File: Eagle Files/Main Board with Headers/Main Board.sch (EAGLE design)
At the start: 34 parts, among them Y1 16MHz

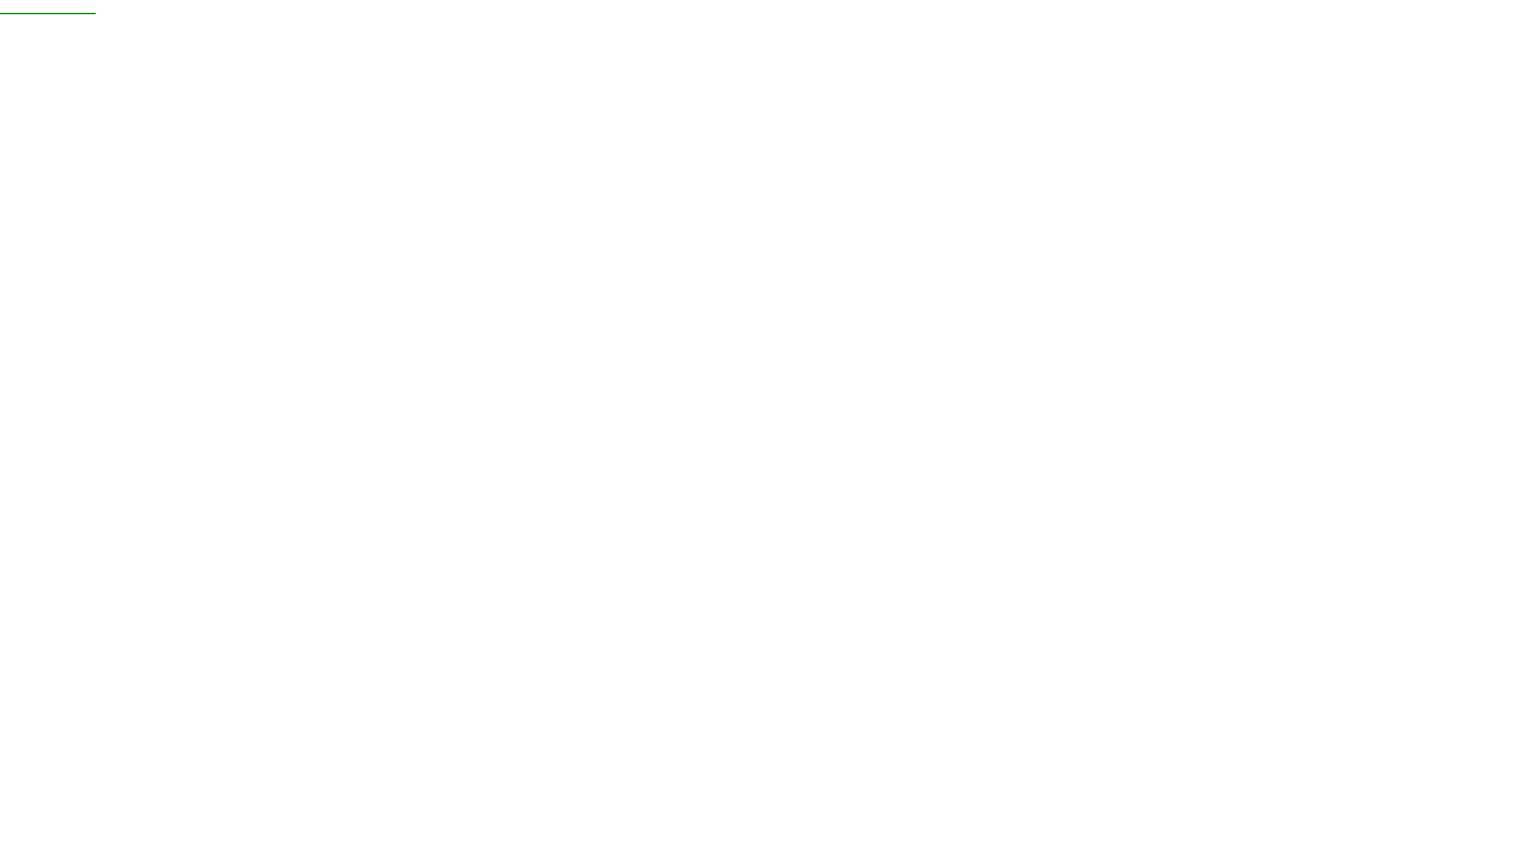
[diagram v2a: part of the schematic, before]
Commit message: Panelized the Radio board and Main Board.
Basically main Board with Headers is being turned into the new Main Board.
I've already attached the SD Card holder.
Next step is to integrate these two boards, instead of just panelizing them.

--Arthur

git-svn-id: http://cd-net.net/CPE496/trunk@116 05b6d0e0-c345-4a8e-a5b7-579c8bd0b646
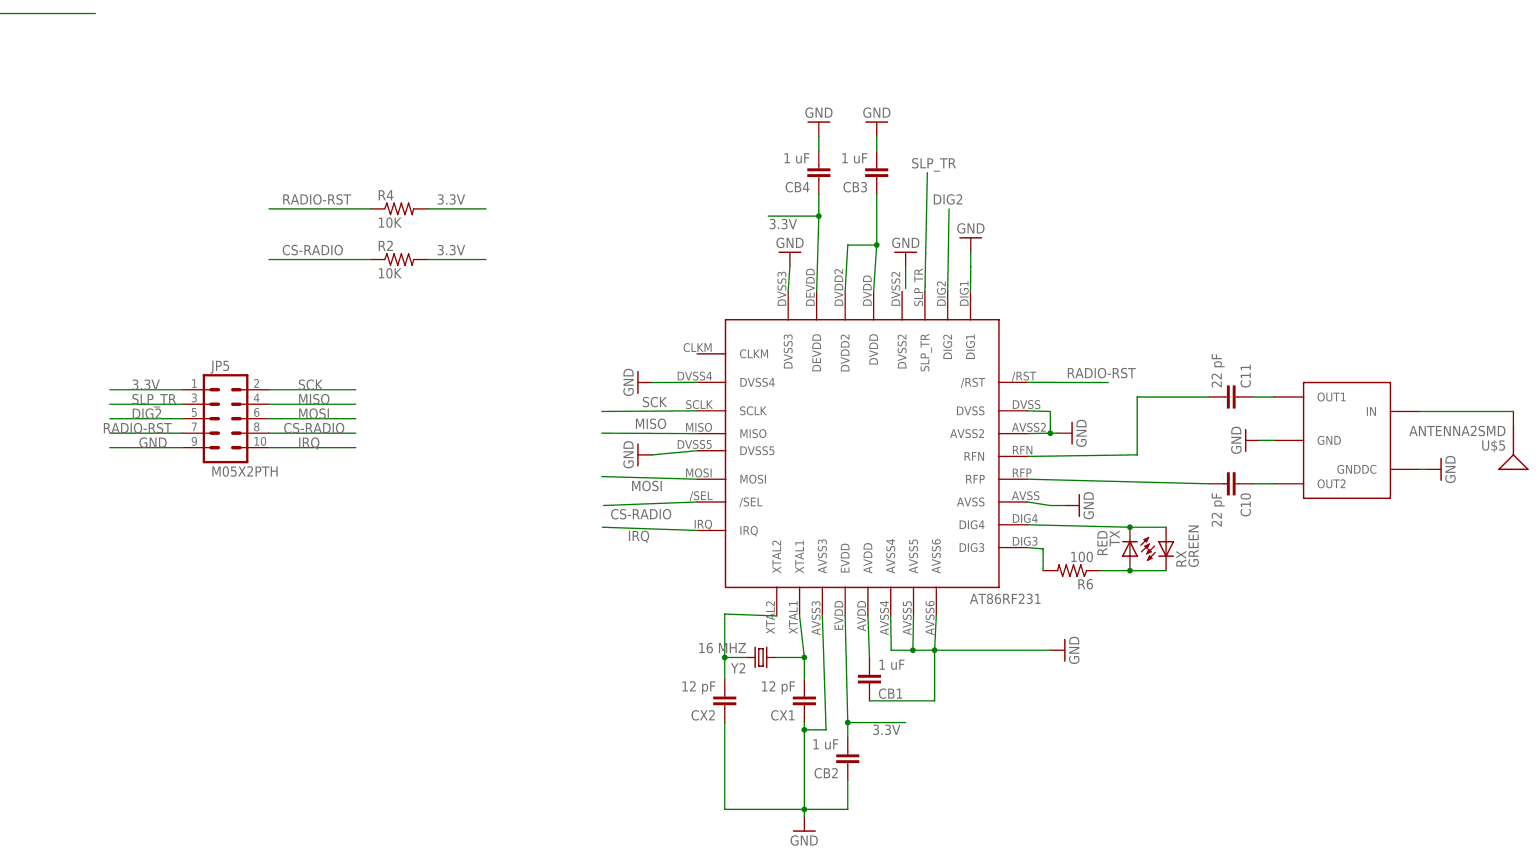
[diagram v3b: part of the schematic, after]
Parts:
- added C10, C11: 22 pF, SparkFun:CAP0603-CAP
- added CB1, CB2, CB3, CB4: 1 uF, SparkFun:CAP0603-CAP
- added CX1, CX2: 12 pF, SparkFun:CAP0603-CAP
- added JP5: M05X2PTH, SparkFun:M05X2PTH
- added R2, R4: 10K, SparkFun:RESISTOR0603-RES
- added R6: 100, SparkFun:RESISTOR0603-RES
- added RX: GREEN, SparkFun:LED0603
- added TX: RED, SparkFun:LED0603
- added U$3: AT86RF231(RADIO)AT86RF231, group10:AT86RF231(RADIO)AT86RF231
- added U$4: WE-BAL, group10:WE-BAL
- added U$5: ANTENNA2SMD, SparkFun:ANTENNA2SMD
- added Y2: 16 MHZ, group10:CRYSTALSMD
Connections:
- new net N$10: CB1.2, U$3.AVDD
- new net N$11: CX1.2, U$3.XTAL1, Y2.1
- new net N$12: CX2.2, U$3.XTAL2, Y2.2
- new net N$13: RX.A, TX.C, U$3.DIG4
- new net N$14: R6.1, RX.C, TX.A
- new net N$15: R6.2, U$3.DIG3
- new net N$16: C10.1, U$4.OUT2
- new net N$17: C11.1, U$4.OUT1
- new net N$18: C11.2, U$3.RFN
- new net N$19: C10.2, U$3.RFP
- new net N$20: U$4.IN, U$5.SIGNAL
- new net N$8: CB3.1, U$3.DVDD, U$3.DVDD2
- net 3.3V: now also CB2.2, CB4.1, JP5.1, R2.2, R4.2, U$3.DEVDD, U$3.EVDD
- net CS-RADIO: now also JP5.8, R2.1, U$3./SEL
- net DIG2: now also JP5.5, U$3.DIG2
- net GND: now also CB1.1, CB2.1, CB3.2, CB4.2, CX1.1, CX2.1, JP5.9, U$3.AVSS, U$3.AVSS2, U$3.AVSS3, U$3.AVSS4, U$3.AVSS5, U$3.AVSS6, U$3.DIG1, U$3.DVSS, U$3.DVSS3, U$3.DVSS4, U$3.DVSS5, U$4.GND, U$4.GNDDC
- net IRQ: now also JP5.10, U$3.IRQ
- net MISO: now also JP5.4, U$3.MISO
- net MOSI: now also JP5.6, U$3.MOSI
- net RADIO-RST: now also JP5.7, R4.1, U$3./RST
- net SCK: now also JP5.2, U$3.SCLK
- net SLP_TR: now also JP5.3, U$3.SLP_TR

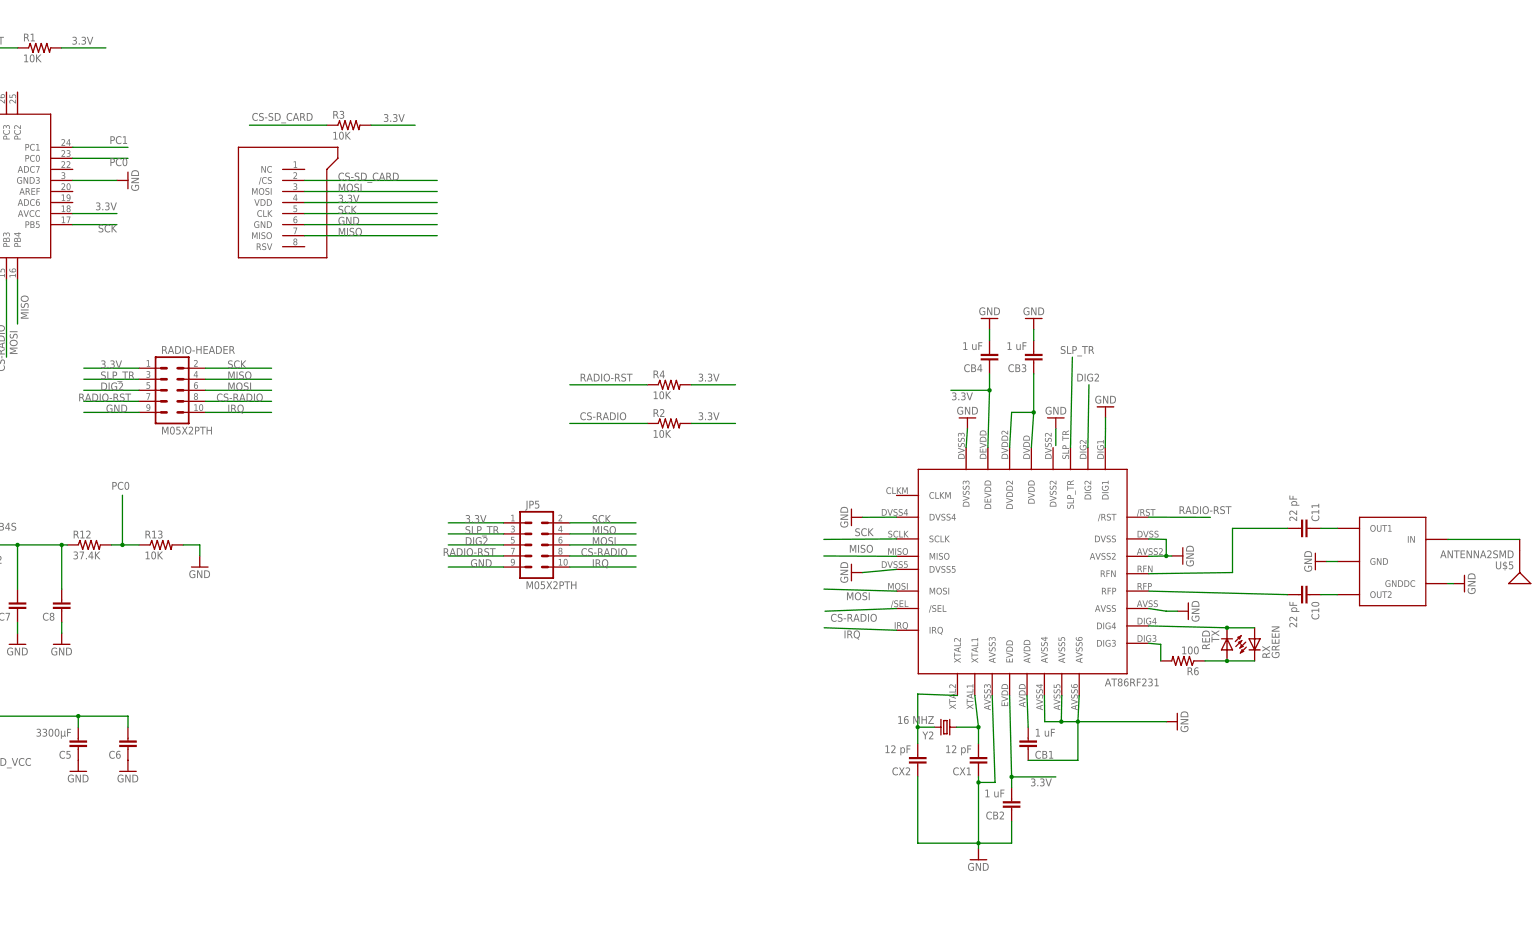
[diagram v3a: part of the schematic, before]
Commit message: Main Board with Headers is now almost ready.
I'm adding the FTDI Module right now.

TODO:
1.  Double check regulator Datasheet.  I think we're missing a capacitor.
2.  Update Radio Module Schematics to incorporate ground plane.
3.  Check if the hall effect sensor can work linearly at 3.3V
4.  Finish Adding FTDI chip and USB connector.

--Arthur

git-svn-id: http://cd-net.net/CPE496/trunk@119 05b6d0e0-c345-4a8e-a5b7-579c8bd0b646
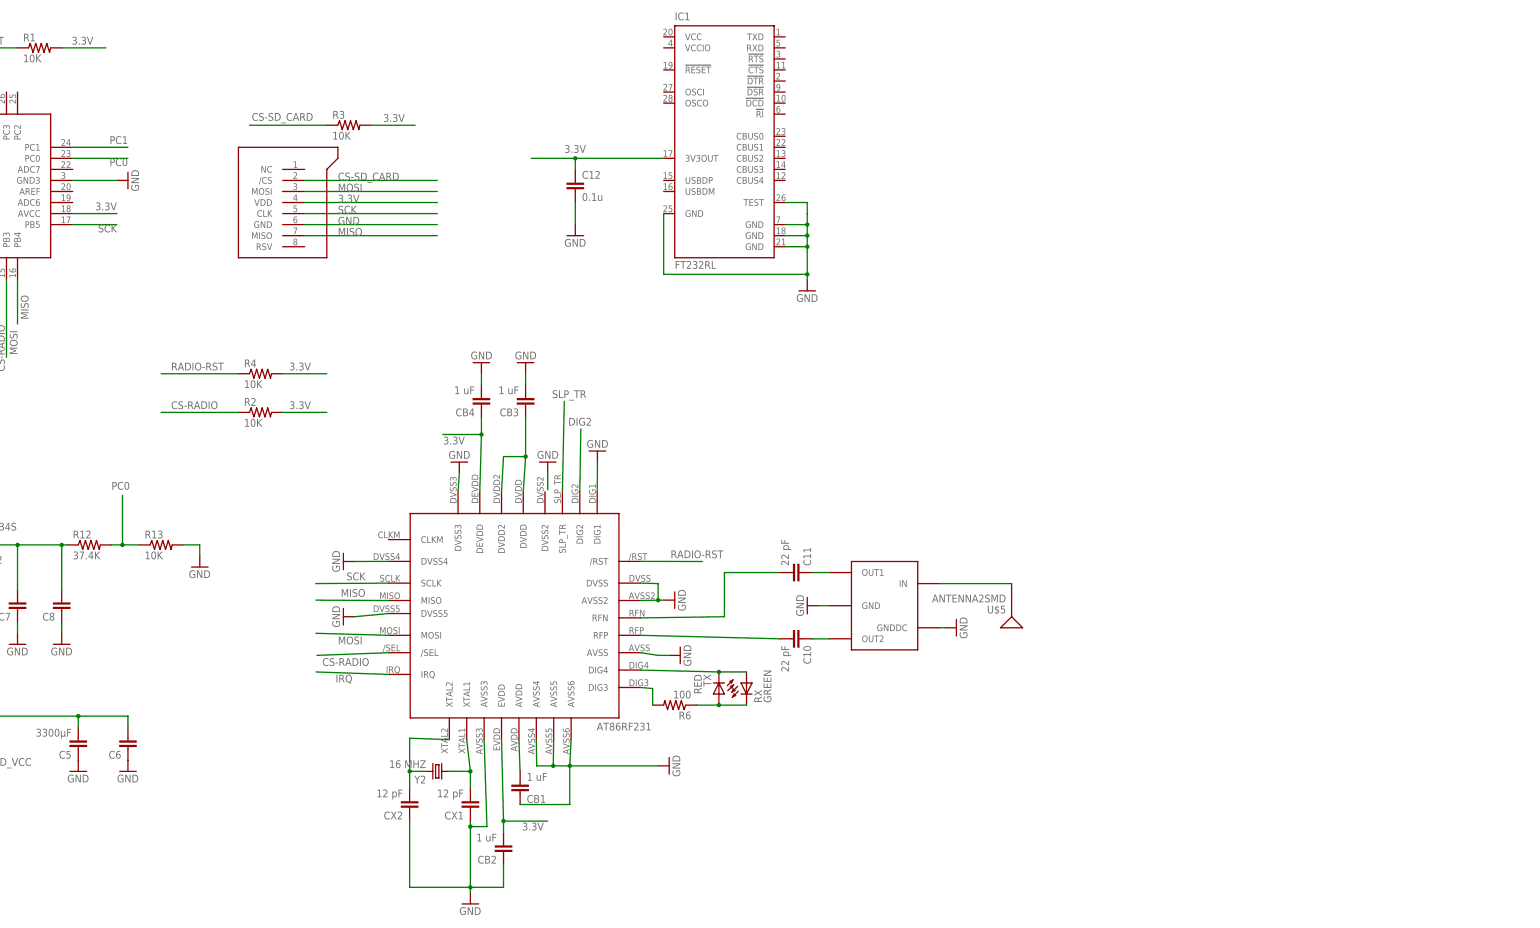
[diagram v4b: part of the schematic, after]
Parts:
- removed JP5, RADIO-HEADER: M05X2PTH, SparkFun:M05X2PTH
- added C12: 0.1u, SparkFun:CAP0603-CAP
- added IC1: FT232RL, ftdichip:FT232RL
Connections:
- net 3.3V: now also C12.1; no longer JP5.1, RADIO-HEADER.1
- net CS-RADIO: no longer JP5.8, RADIO-HEADER.8
- net DIG2: no longer JP5.5, RADIO-HEADER.5
- net GND: now also C12.2, IC1.GND, IC1.GND@1, IC1.GND@2, IC1.GND@A, IC1.TEST; no longer JP5.9, RADIO-HEADER.9
- net IRQ: no longer JP5.10, RADIO-HEADER.10
- net MISO: no longer JP5.4, RADIO-HEADER.4
- net MOSI: no longer JP5.6, RADIO-HEADER.6
- net RADIO-RST: no longer JP5.7, RADIO-HEADER.7
- net SCK: no longer JP5.2, RADIO-HEADER.2
- net SLP_TR: no longer JP5.3, RADIO-HEADER.3
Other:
- moved on the sheet: C10, C11, CB1, CB2, CB3, CB4, CX1, CX2, R2, R4, R6, RX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
